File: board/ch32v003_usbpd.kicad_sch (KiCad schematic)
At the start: 21 parts, among them J1 USB_C_Receptacle_USB2.0, J2 Conn_01x04_Pin, J3 VOUT, U1 CH32V003F4P6, U2 HT75xx-1-SOT89

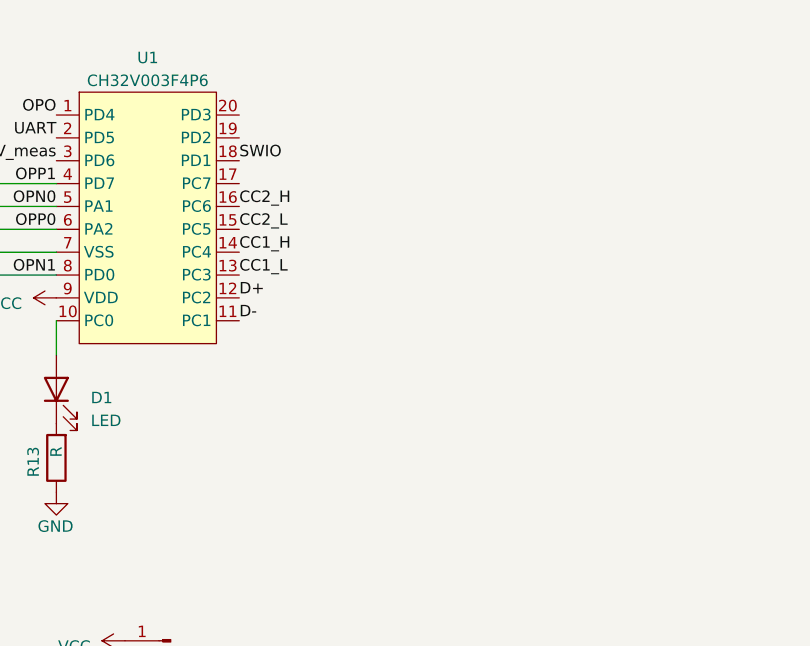
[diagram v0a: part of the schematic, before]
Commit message: Add test points to board
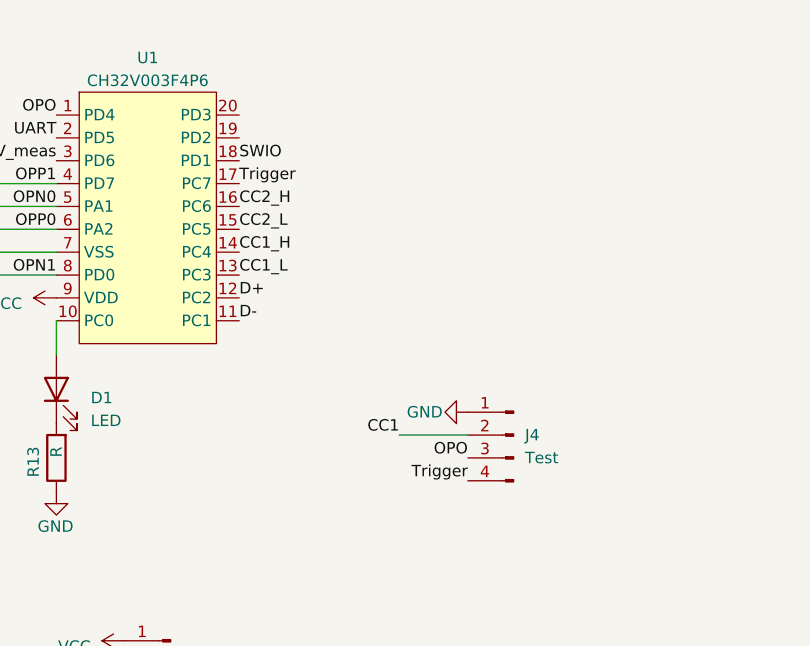
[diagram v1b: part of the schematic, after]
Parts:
- added J4: Test, Connector_PinHeader_2.54mm:PinHeader_1x04_P2.54mm_Vertical, symbol Connector:Conn_01x04_Pin
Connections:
- net CC1: now also J4.2 (Pin_2)
- net GND: now also J4.1 (Pin_1)
- net OPO: now also J4.3 (Pin_3)
- net Trigger: now reaches U1.17 (PC7)
- net Trigger: now also J4.4 (Pin_4)
